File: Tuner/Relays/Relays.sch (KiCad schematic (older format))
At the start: 69 parts, among them J1 Conn_01x03, J10 Conn_01x02, J11 Conn_01x02, J12 Conn_01x01, J13 Conn_01x01, J14 Conn_01x01, J15 Conn_01x01, J16 Conn_01x02, J17 Conn_02x10_Odd_Even, J18 Conn_01x02, J19 Conn_01x03, J2 Conn_01x03, J3 Conn_01x03, J4 Conn_01x03, J5 Conn_01x03, J6 Conn_01x03, J7 Conn_01x03, J8 Conn_01x02, J9 Conn_01x02

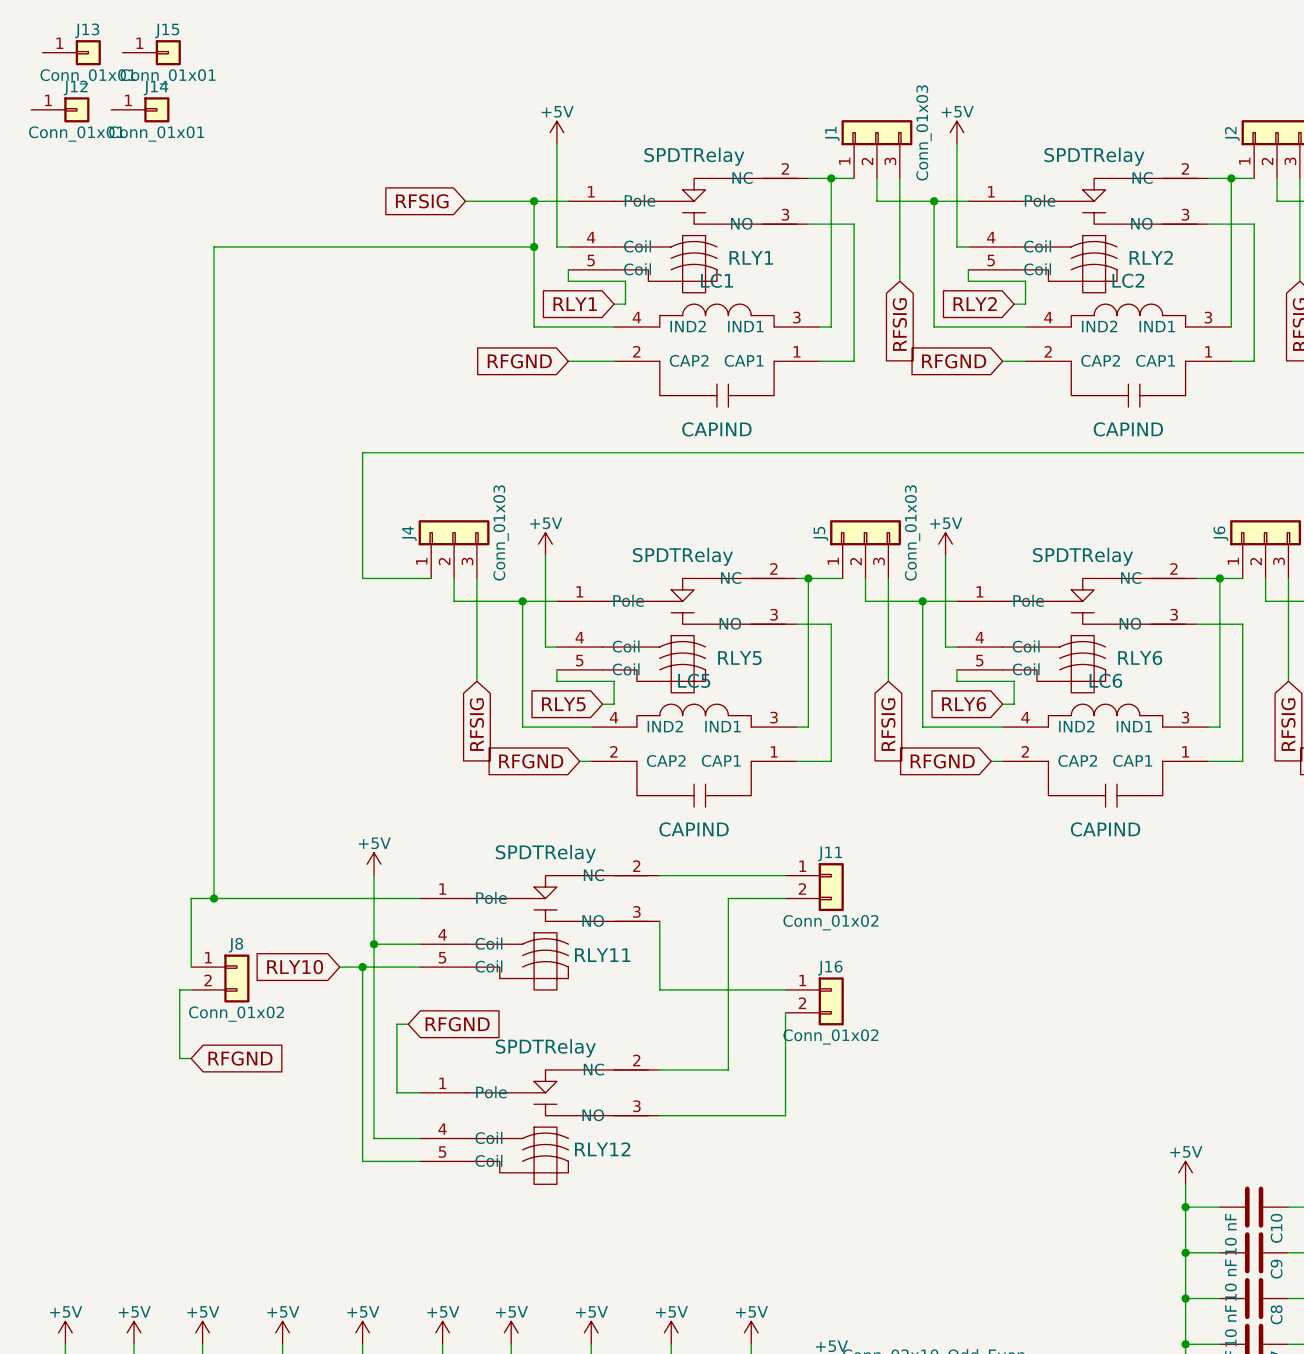
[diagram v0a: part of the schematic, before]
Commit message: JLCPCB submitted RelayControl version
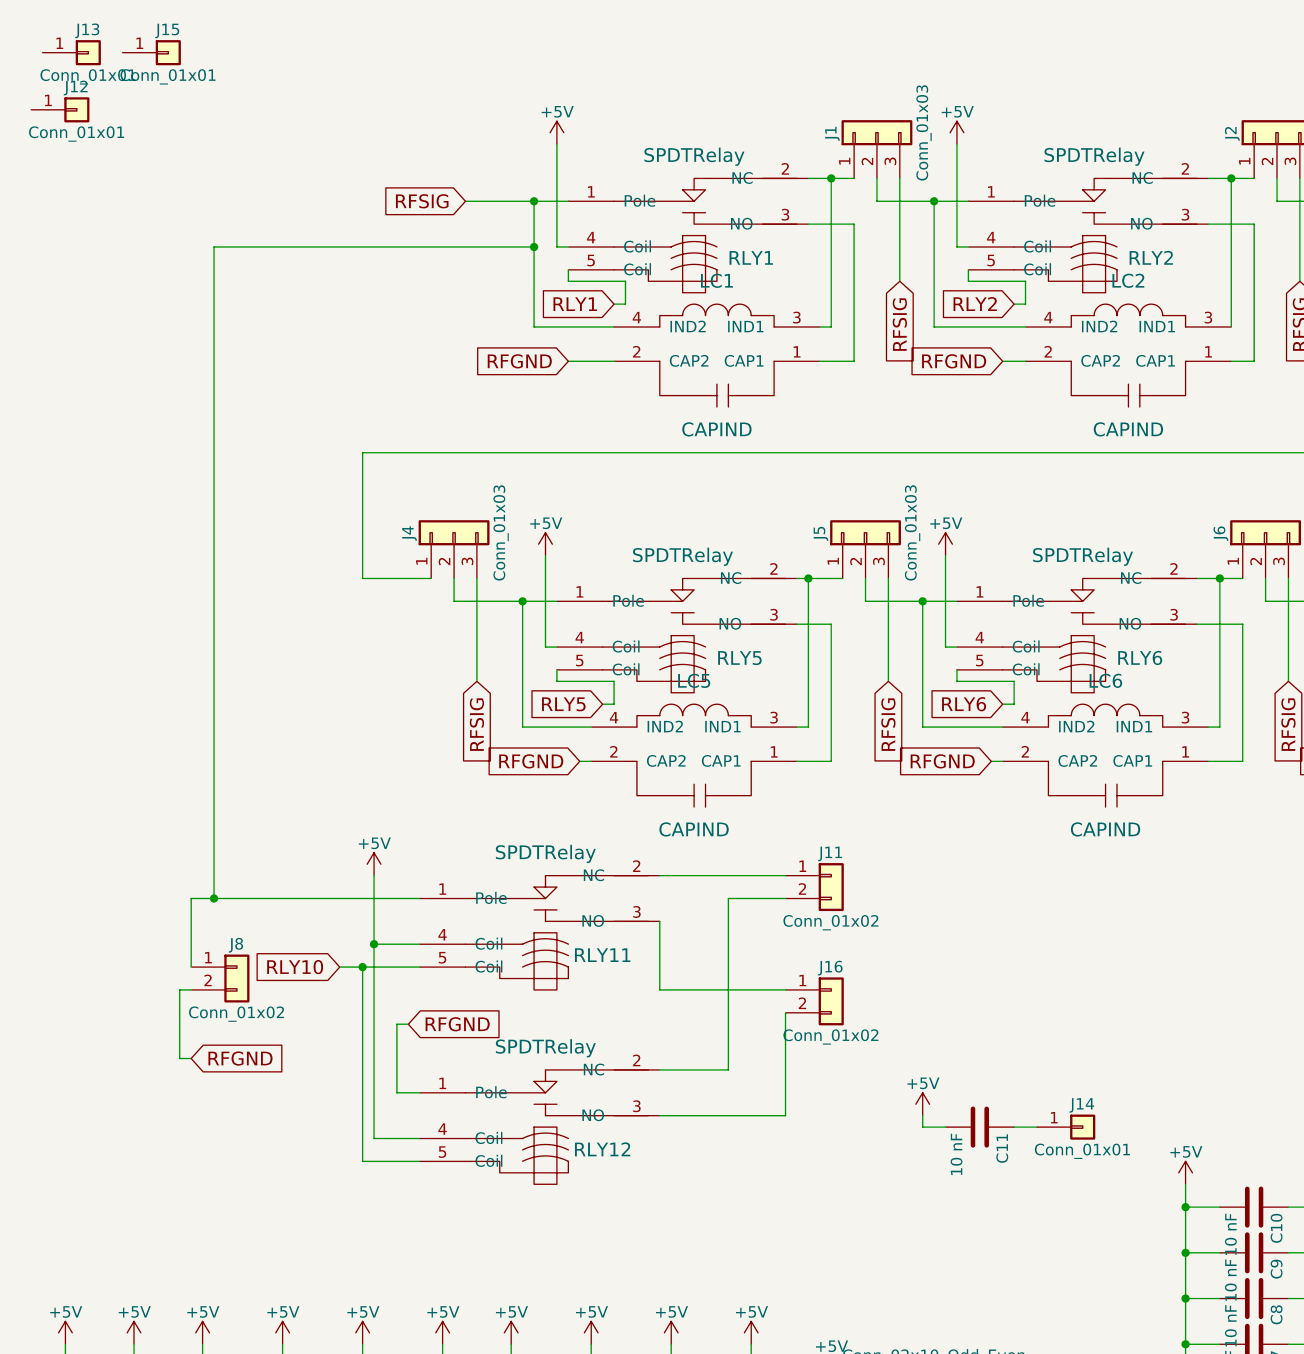
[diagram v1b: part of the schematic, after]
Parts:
- added C11: 10 nF, Capacitors_THT:C_Disc_D5.0mm_W2.5mm_P2.50mm, symbol C
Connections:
- net +5V: now also C11.2
- net at J14.1 (Pin_1): now also C11.1
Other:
- moved on the sheet: J14
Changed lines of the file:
@@
 $EndComp
 $Comp
-L +5V #PWR01
+L +5V #PWR9
 U 1 1 5B1A3BAF
 P 2950 2950
-F 0 "#PWR01" H 2950 2800 50  0001 C CNN
+F 0 "#PWR9" H 2950 2800 50  0001 C CNN
 F 1 "+5V" H 2950 3090 50  0000 C CNN
 F 2 "" H 2950 2950 50  0001 C CNN
@@
 $EndComp
 $Comp
-L +5V #PWR02
+L +5V #PWR16
 U 1 1 5B1A3CC8
 P 4700 2950
-F 0 "#PWR02" H 4700 2800 50  0001 C CNN
+F 0 "#PWR16" H 4700 2800 50  0001 C CNN
 F 1 "+5V" H 4700 3090 50  0000 C CNN
 F 2 "" H 4700 2950 50  0001 C CNN
@@
 $EndComp
 $Comp
-L +5V #PWR03
+L +5V #PWR19
 U 1 1 5B1A3D42
 P 6450 2900
-F 0 "#PWR03" H 6450 2750 50  0001 C CNN
+F 0 "#PWR19" H 6450 2750 50  0001 C CNN
 F 1 "+5V" H 6450 3040 50  0000 C CNN
 F 2 "" H 6450 2900 50  0001 C CNN
@@
 $EndComp
 $Comp
-L +5V #PWR04
+L +5V #PWR22
 U 1 1 5B1A3DBC
 P 8100 4450
-F 0 "#PWR04" H 8100 4300 50  0001 C CNN
+F 0 "#PWR22" H 8100 4300 50  0001 C CNN
 F 1 "+5V" H 8100 4590 50  0000 C CNN
 F 2 "" H 8100 4450 50  0001 C CNN
@@
 $EndComp
 $Comp
-L +5V #PWR05
+L +5V #PWR23
 U 1 1 5B1A4C3F
 P 8250 1200
-F 0 "#PWR05" H 8250 1050 50  0001 C CNN
+F 0 "#PWR23" H 8250 1050 50  0001 C CNN
 F 1 "+5V" H 8250 1340 50  0000 C CNN
 F 2 "" H 8250 1200 50  0001 C CNN
@@
 $EndComp
 $Comp
-L +5V #PWR06
+L +5V #PWR20
 U 1 1 5B1A4CB9
 P 6500 1200
-F 0 "#PWR06" H 6500 1050 50  0001 C CNN
+F 0 "#PWR20" H 6500 1050 50  0001 C CNN
 F 1 "+5V" H 6500 1340 50  0000 C CNN
 F 2 "" H 6500 1200 50  0001 C CNN
@@
 $EndComp
 $Comp
-L +5V #PWR07
+L +5V #PWR17
 U 1 1 5B1A4D33
 P 4750 1150
-F 0 "#PWR07" H 4750 1000 50  0001 C CNN
+F 0 "#PWR17" H 4750 1000 50  0001 C CNN
 F 1 "+5V" H 4750 1290 50  0000 C CNN
 F 2 "" H 4750 1150 50  0001 C CNN
@@
 $EndComp
 $Comp
-L +5V #PWR08
+L +5V #PWR10
 U 1 1 5B1A4DAD
 P 3000 1150
-F 0 "#PWR08" H 3000 1000 50  0001 C CNN
+F 0 "#PWR10" H 3000 1000 50  0001 C CNN
 F 1 "+5V" H 3000 1290 50  0000 C CNN
 F 2 "" H 3000 1150 50  0001 C CNN
@@
 L Conn_01x01 J14
 U 1 1 5B198288
-P 1250 1000
-F 0 "J14" H 1250 1100 50  0000 C CNN
-F 1 "Conn_01x01" H 1250 900 50  0000 C CNN
-F 2 "Connectors:1pin" H 1250 1000 50  0001 C CNN
-F 3 "" H 1250 1000 50  0001 C CNN
-	1    1250 1000
+P 5300 5450
+F 0 "J14" H 5300 5550 50  0000 C CNN
+F 1 "Conn_01x01" H 5300 5350 50  0000 C CNN
+F 2 "Connectors:1pin" H 5300 5450 50  0001 C CNN
+F 3 "" H 5300 5450 50  0001 C CNN
+	1    5300 5450
 	1    0    0    -1
 $EndComp
@@
 $EndComp
 $Comp
-L +5V #PWR09
+L +5V #PWR3
 U 1 1 5B25DE9C
 P 1450 6400
-F 0 "#PWR09" H 1450 6250 50  0001 C CNN
+F 0 "#PWR3" H 1450 6250 50  0001 C CNN
 F 1 "+5V" H 1450 6540 50  0000 C CNN
 F 2 "" H 1450 6400 50  0001 C CNN
@@
 $EndComp
 $Comp
-L +5V #PWR010
+L +5V #PWR4
 U 1 1 5B25F712
 P 1800 6400
-F 0 "#PWR010" H 1800 6250 50  0001 C CNN
+F 0 "#PWR4" H 1800 6250 50  0001 C CNN
 F 1 "+5V" H 1800 6540 50  0000 C CNN
 F 2 "" H 1800 6400 50  0001 C CNN
@@
 $EndComp
 $Comp
-L +5V #PWR011
+L +5V #PWR5
 U 1 1 5B25F91B
 P 2150 6400
-F 0 "#PWR011" H 2150 6250 50  0001 C CNN
+F 0 "#PWR5" H 2150 6250 50  0001 C CNN
 F 1 "+5V" H 2150 6540 50  0000 C CNN
 F 2 "" H 2150 6400 50  0001 C CNN
@@
 $EndComp
 $Comp
-L +5V #PWR012
+L +5V #PWR7
 U 1 1 5B25F931
 P 2500 6400
-F 0 "#PWR012" H 2500 6250 50  0001 C CNN
+F 0 "#PWR7" H 2500 6250 50  0001 C CNN
 F 1 "+5V" H 2500 6540 50  0000 C CNN
 F 2 "" H 2500 6400 50  0001 C CNN
@@
 $EndComp
 $Comp
-L +5V #PWR013
+L +5V #PWR8
 U 1 1 5B25FB4D
 P 2800 6400
-F 0 "#PWR013" H 2800 6250 50  0001 C CNN
+F 0 "#PWR8" H 2800 6250 50  0001 C CNN
 F 1 "+5V" H 2800 6540 50  0000 C CNN
 F 2 "" H 2800 6400 50  0001 C CNN
@@
 $EndComp
 $Comp
-L +5V #PWR014
+L +5V #PWR11
 U 1 1 5B25FB63
 P 3150 6400
-F 0 "#PWR014" H 3150 6250 50  0001 C CNN
+F 0 "#PWR11" H 3150 6250 50  0001 C CNN
 F 1 "+5V" H 3150 6540 50  0000 C CNN
 F 2 "" H 3150 6400 50  0001 C CNN
@@
 $EndComp
 $Comp
-L +5V #PWR015
+L +5V #PWR12
 U 1 1 5B25FB79
 P 3500 6400
-F 0 "#PWR015" H 3500 6250 50  0001 C CNN
+F 0 "#PWR12" H 3500 6250 50  0001 C CNN
 F 1 "+5V" H 3500 6540 50  0000 C CNN
 F 2 "" H 3500 6400 50  0001 C CNN
@@
 $EndComp
 $Comp
-L +5V #PWR016
+L +5V #PWR13
 U 1 1 5B25FB8F
 P 3850 6400
-F 0 "#PWR016" H 3850 6250 50  0001 C CNN
+F 0 "#PWR13" H 3850 6250 50  0001 C CNN
 F 1 "+5V" H 3850 6540 50  0000 C CNN
 F 2 "" H 3850 6400 50  0001 C CNN
@@
 	5050 6550 4900 6550
 $Comp
-L +5V #PWR017
+L +5V #PWR14
 U 1 1 5B89A678
 P 4200 6550
-F 0 "#PWR017" H 4200 6400 50  0001 C CNN
+F 0 "#PWR14" H 4200 6400 50  0001 C CNN
 F 1 "+5V" H 4200 6690 50  0000 C CNN
 F 2 "" H 4200 6550 50  0001 C CNN
@@
 $EndComp
 $Comp
-L +5V #PWR018
+L +5V #PWR2
 U 1 1 5B89BB19
 P 1150 6400
-F 0 "#PWR018" H 1150 6250 50  0001 C CNN
+F 0 "#PWR2" H 1150 6250 50  0001 C CNN
 F 1 "+5V" H 1150 6540 50  0000 C CNN
 F 2 "" H 1150 6400 50  0001 C CNN
@@
 $EndComp
 $Comp
-L +5V #PWR019
+L +5V #PWR1
 U 1 1 5B89BBCB
 P 850 6400
-F 0 "#PWR019" H 850 6250 50  0001 C CNN
+F 0 "#PWR1" H 850 6250 50  0001 C CNN
 F 1 "+5V" H 850 6540 50  0000 C CNN
 F 2 "" H 850 6400 50  0001 C CNN
@@
 Connection ~ 5750 6000
 $Comp
-L +5V #PWR020
+L +5V #PWR18
 U 1 1 5B89FB34
 P 5750 5700
-F 0 "#PWR020" H 5750 5550 50  0001 C CNN
+F 0 "#PWR18" H 5750 5550 50  0001 C CNN
 F 1 "+5V" H 5750 5840 50  0000 C CNN
 F 2 "" H 5750 5700 50  0001 C CNN
@@
 RLY8
 $Comp
-L +5V #PWR021
+L +5V #PWR21
 U 1 1 5B8A1B7B
 P 8100 2900
-F 0 "#PWR021" H 8100 2750 50  0001 C CNN
+F 0 "#PWR21" H 8100 2750 50  0001 C CNN
 F 1 "+5V" H 8100 3040 50  0000 C CNN
 F 2 "" H 8100 2900 50  0001 C CNN
@@
 $EndComp
 $Comp
-L +5V #PWR022
+L +5V #PWR6
 U 1 1 5B8A2542
 P 2200 4350
-F 0 "#PWR022" H 2200 4200 50  0001 C CNN
+F 0 "#PWR6" H 2200 4200 50  0001 C CNN
 F 1 "+5V" H 2200 4490 50  0000 C CNN
 F 2 "" H 2200 4350 50  0001 C CNN
@@
 	-1   0    0    1
 $EndComp
+$Comp
+L C C11
+U 1 1 5B97C52E
+P 4850 5450
+F 0 "C11" H 4875 5550 50  0000 L CNN
+F 1 "10 nF" H 4875 5350 50  0000 L CNN
+F 2 "Capacitors_THT:C_Disc_D5.0mm_W2.5mm_P2.50mm" H 4888 5300 50  0001 C CNN
+F 3 "" H 4850 5450 50  0001 C CNN
+	1    4850 5450
+	0    1    1    0
+$EndComp
+$Comp
+L +5V #PWR15
+U 1 1 5B97C780
+P 4600 5400
+F 0 "#PWR15" H 4600 5250 50  0001 C CNN
+F 1 "+5V" H 4600 5540 50  0000 C CNN
+F 2 "" H 4600 5400 50  0001 C CNN
+F 3 "" H 4600 5400 50  0001 C CNN
+	1    4600 5400
+	1    0    0    -1
+$EndComp
+Wire Wire Line
+	4600 5400 4600 5450
+Wire Wire Line
+	4600 5450 4700 5450
+Wire Wire Line
+	5100 5450 5000 5450
 $EndSCHEMATC

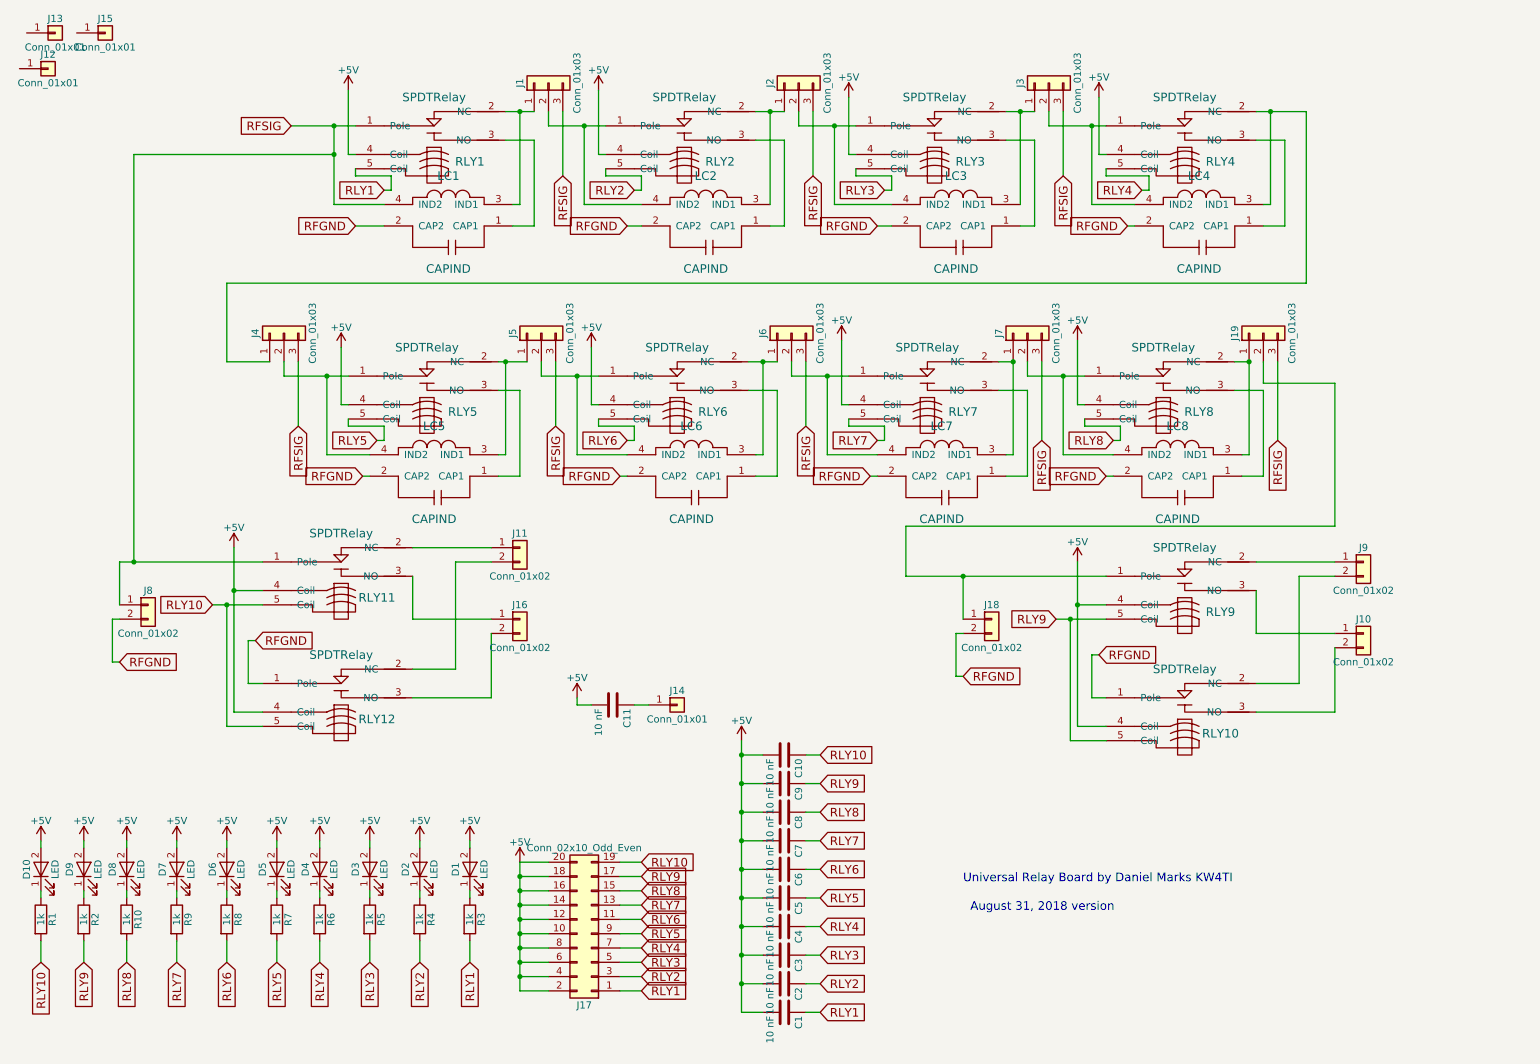
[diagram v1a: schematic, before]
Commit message: JLCPCB order 09232018 - improved grounding - improved I2C cabling - NEO7M port - support for common mode chokes - relay board now has capacitors on all coils
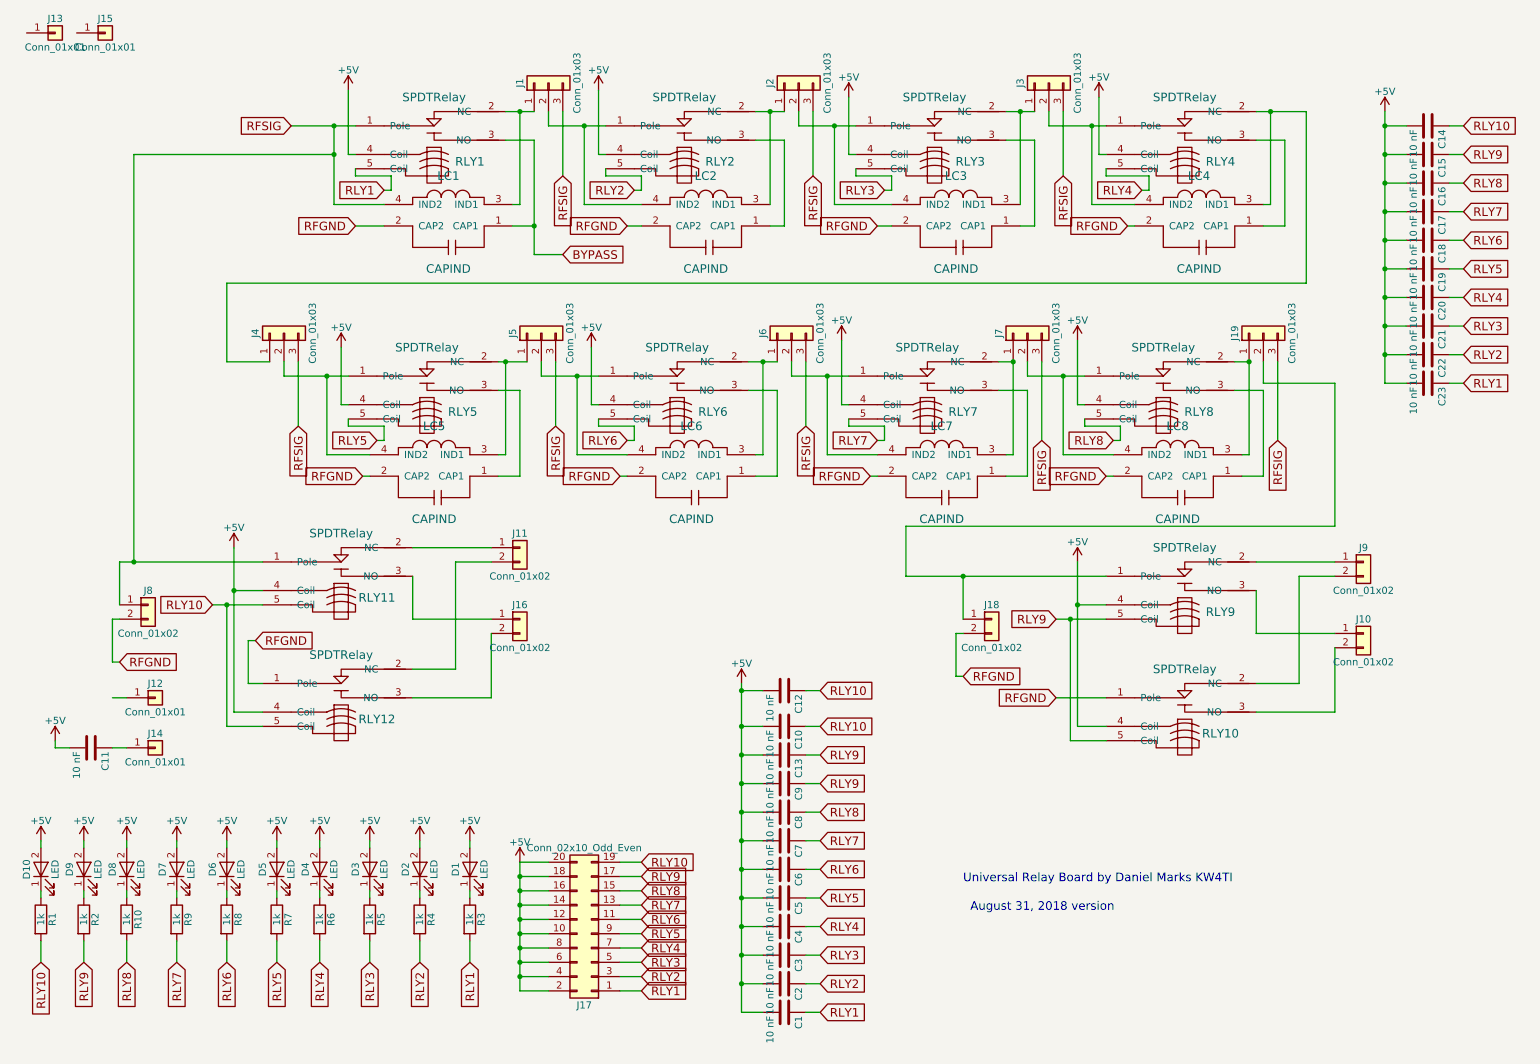
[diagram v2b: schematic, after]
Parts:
- added C12, C13, C14, C15, C16, C17, C18, C19, C20, C21, C22, C23: 10 nF, Capacitors_THT:C_Disc_D5.0mm_W2.5mm_P2.50mm, symbol C
- J17: footprint (none) -> Pin_Headers:Pin_Header_Straight_2x10_Pitch2.54mm
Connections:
- net +5V: now also C12.2, C13.2, C14.2, C15.2, C16.2, C17.2, C18.2, C19.2, C20.2, C21.2, C22.2, C23.2
- net RLY1: now also C23.1
- net RLY10: now also C12.1, C14.1
- net RLY2: now also C22.1
- net RLY3: now also C21.1
- net RLY4: now also C20.1
- net RLY5: now also C19.1
- net RLY6: now also C18.1
- net RLY7: now also C17.1
- net RLY8: now also C16.1
- net RLY9: now also C13.1, C15.1
- net BYPASS: now reaches LC1.1 (CAP1), RLY1.3 (NO)
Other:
- moved on the sheet: C10, C11, J12, J14
